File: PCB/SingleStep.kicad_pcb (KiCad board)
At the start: 2 copper layers, 63.5 x 30.5 mm, 19 parts, among them IC1 ATTINY24A-P, P1 INPUT, P2 OUTPUT, P3 Light, P4 IR

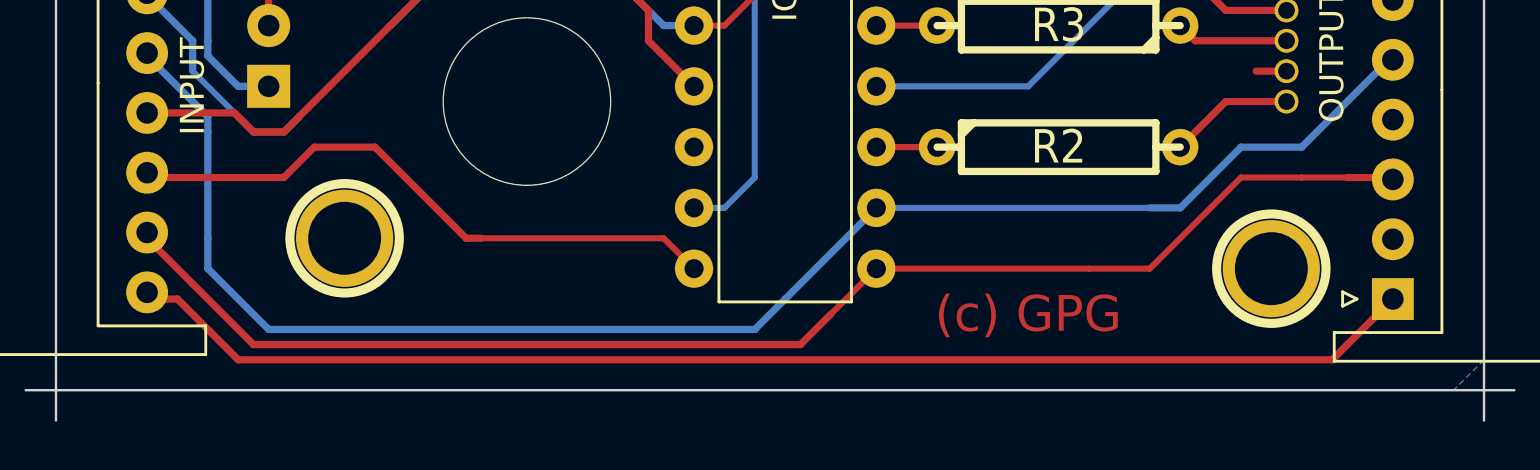
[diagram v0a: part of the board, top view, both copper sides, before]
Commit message: Add "Last step" jumper
Also add version information to PCB
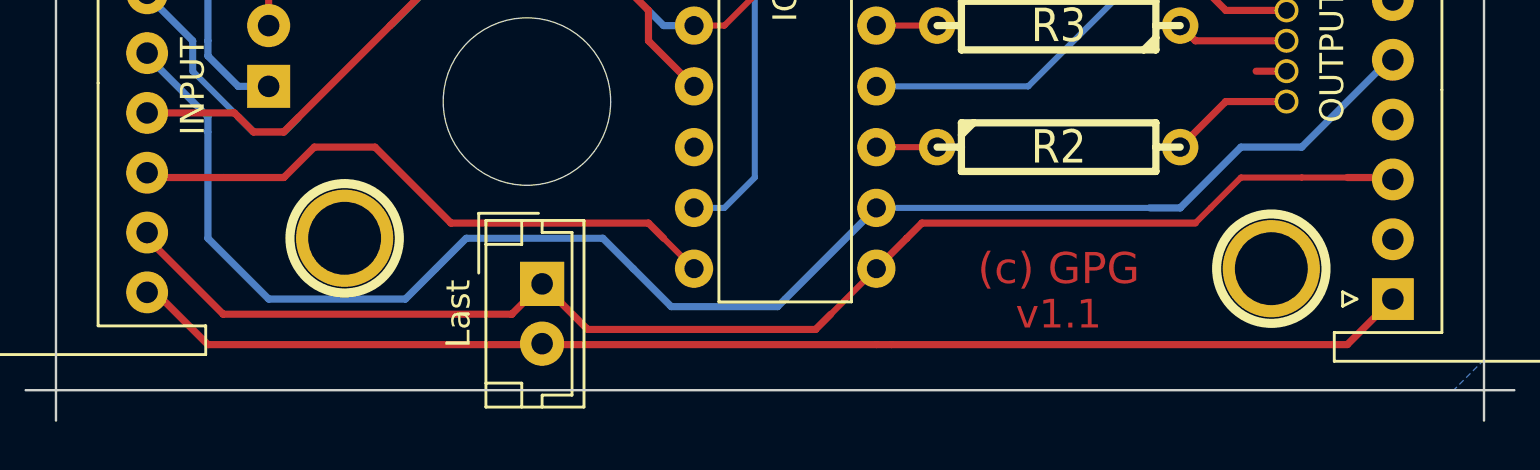
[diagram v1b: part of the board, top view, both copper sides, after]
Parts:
- added P5: Last, Connectors_JST:JST_EH_B02B-EH-A_02x2.50mm_Straight, F.Cu at (31.8, 36.2)
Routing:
- net /MISO: track 56.8 -> 57.6 mm
- net CLK: track 65.4 -> 65.9 mm
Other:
- board text added: "v1.1"

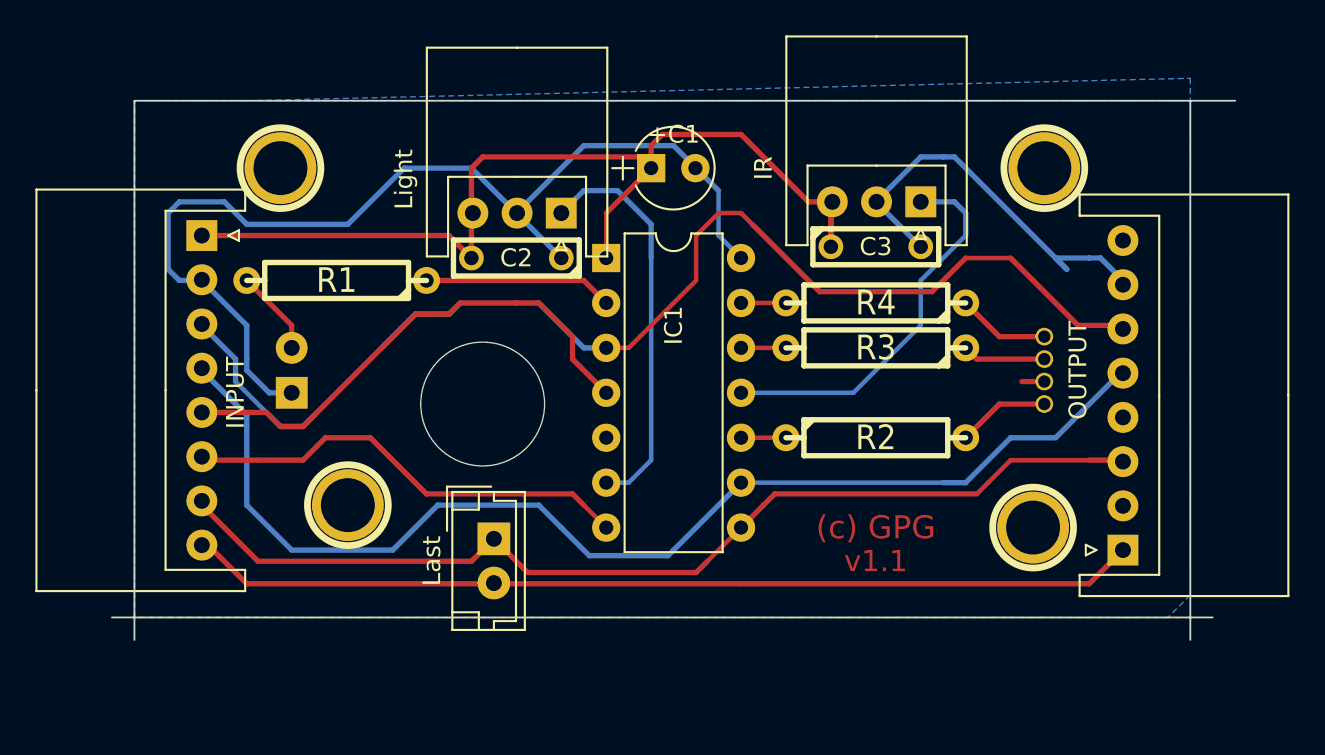
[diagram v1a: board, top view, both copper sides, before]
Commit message: Change PCB to SMD
Change most components to SMD components.
Add LM7805 Voltage regulator.
Add automatic last step detection.
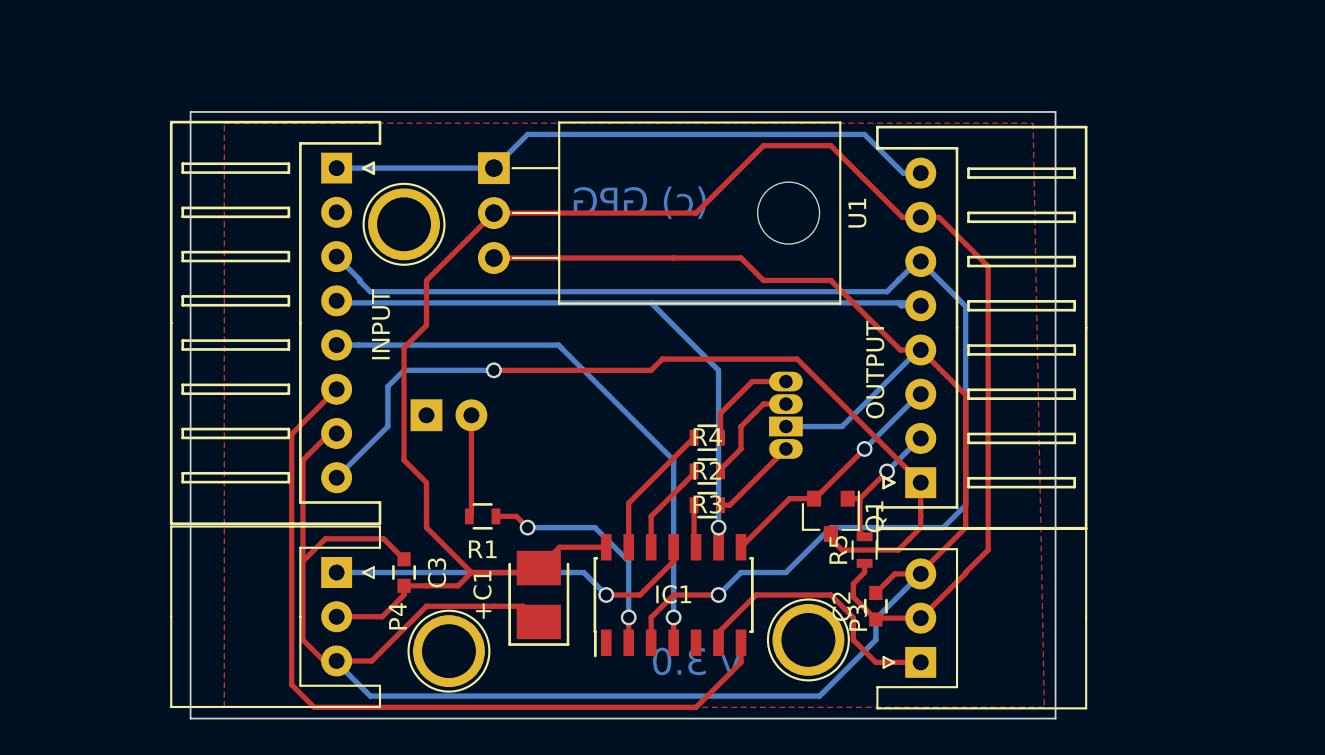
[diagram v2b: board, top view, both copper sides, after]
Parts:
- removed ? (x4): , 1pin
- removed ?: , Screw Hole
- removed P5: Last, Connectors_JST:JST_EH_B02B-EH-A_02x2.50mm_Straight
- added Q1: MMBT3906, TO_SOT_Packages_SMD:SOT-23, F.Cu at (50.8, 34.9)
- added R5: R, Resistors_SMD:R_0603, F.Cu at (52.7, 36.8)
- added REF**: 1pin, Connect:1pin, F.Cu at (26.7, 18.4)
- added REF**: 1pin, Connect:1pin, F.Cu at (29.2, 42.5)
- added REF**: 1pin, Connect:1pin, F.Cu at (49.5, 41.9)
- added U1: LM7805, TO_SOT_Packages_THT:TO-220_Horizontal, F.Cu at (31.8, 15.2)
- +C1: footprint Capacitors_ThroughHole:CP_Radial_Tantal_D4.5mm_P2.50mm -> Capacitors_Tantalum_SMD:Tantalum_Case-B_EIA-3528-21_Reflow
- C2, C3: footprint C2 -> Capacitors_SMD:C_0603
- IC1: footprint Housings_DIP:DIP-14_W7.62mm -> Housings_SOIC:SOIC-14_3.9x8.7mm_Pitch1.27mm
- LED2: footprint LED5_RGB_long -> LEDs:LED-RGB-5MM_Common_Cathode
- R1, R2, R3, R4: footprint R4 -> Resistors_SMD:R_0603
- moved P4 39.1 mm to (22.9, 38.1), turned to 270 degrees
- moved P3 32.5 mm to (55.9, 43.2), turned to 90 degrees
- moved C3 32.4 mm to (26.7, 38.1), turned to 270 degrees
- moved C2 28.3 mm to (53.3, 40.0), turned to 90 degrees
- moved +C1 25.0 mm to (34.3, 39.4), turned to 90 degrees
- moved IC1 19.4 mm to (41.9, 39.4), turned to 90 degrees
- moved R1 15.7 mm to (31.1, 34.9)
- moved LED2 15.3 mm to (48.3, 31.1), turned to 0 degrees
- moved R4 12.2 mm to (43.8, 30.5)
- moved P2 12.0 mm to (55.9, 33.0)
- moved R3 11.8 mm to (43.8, 32.4)
- moved R2 10.3 mm to (43.8, 34.3)
- moved P1 8.52 mm to (22.9, 15.2)
- moved D1 7.73 mm to (27.9, 29.2), turned to 0 degrees
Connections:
- net CLK renamed /CLK
- +C1 pad 1: /Vcc -> Net-(+C1-Pad1)
- C2 pad 2: /Vcc -> Net-(+C1-Pad1)
- C3 pad 1: /Vcc -> Net-(+C1-Pad1)
- IC1 pad 1: /Vcc -> Net-(IC1-Pad1)
- LED2 pad 2: /Vcc -> Net-(+C1-Pad1)
- P1 pad 1: /Vcc -> /Vin
- P1 pad 7: /MISO -> Net-(+C1-Pad1)
- P2 pad 4: /Vcc -> Net-(+C1-Pad1)
- P2 pad 8: /Vcc -> /Vin
- P3 pad 3: /Vcc -> Net-(+C1-Pad1)
- P4 pad 3: /Vcc -> Net-(+C1-Pad1)
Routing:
- net Net-(+C1-Pad1): track 0.00 -> 126.3 mm
- net /Vcc: track 57.3 -> 0.00 mm
- net /MISO: track 57.6 -> 13.7 mm, vias 0 -> 1
- net /Vin: track 0.00 -> 34.7 mm
- net /MOSI: track 25.5 -> 46.1 mm
- net /GND: track 83.5 -> 101.6 mm
- net /CLK: track 65.9 -> 49.9 mm, vias 0 -> 1
- net Net-(P2-Pad2): track 0.00 -> 8.58 mm, vias 0 -> 1
- net Net-(IC1-Pad6): track 22.8 -> 15.2 mm
- net Net-(IC1-Pad13): track 2.54 -> 7.72 mm
- net /Upstream MISO: track 53.8 -> 49.0 mm, vias 0 -> 1
- net /SS: track 68.1 -> 71.7 mm, vias 0 -> 1
- net /RST: track 28.9 -> 32.1 mm, vias 0 -> 1
- net Net-(IC1-Pad12): track 2.54 -> 5.29 mm
- net Net-(IC1-Pad2): track 10.7 -> 13.2 mm, vias 0 -> 2
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- added copper zone on F.Cu, net /GND
- removed copper zone on B.Cu, net /GND
- removed copper zone on F.Cu, net /Vcc
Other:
- board size 63.5 x 30.5 mm -> 48.9 x 34.3 mm
- board text added: "v 3.0"
- board text removed: "v1.1"
